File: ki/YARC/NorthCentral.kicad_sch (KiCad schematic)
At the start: 10 parts, among them U102 74HC245, U103 74HC245, U106 74LS139, U128 74LS157, U132 74LS157, U133 74LS21, U134 74LS32, U138 74LS14, U146 74LS574, U93 74LS32

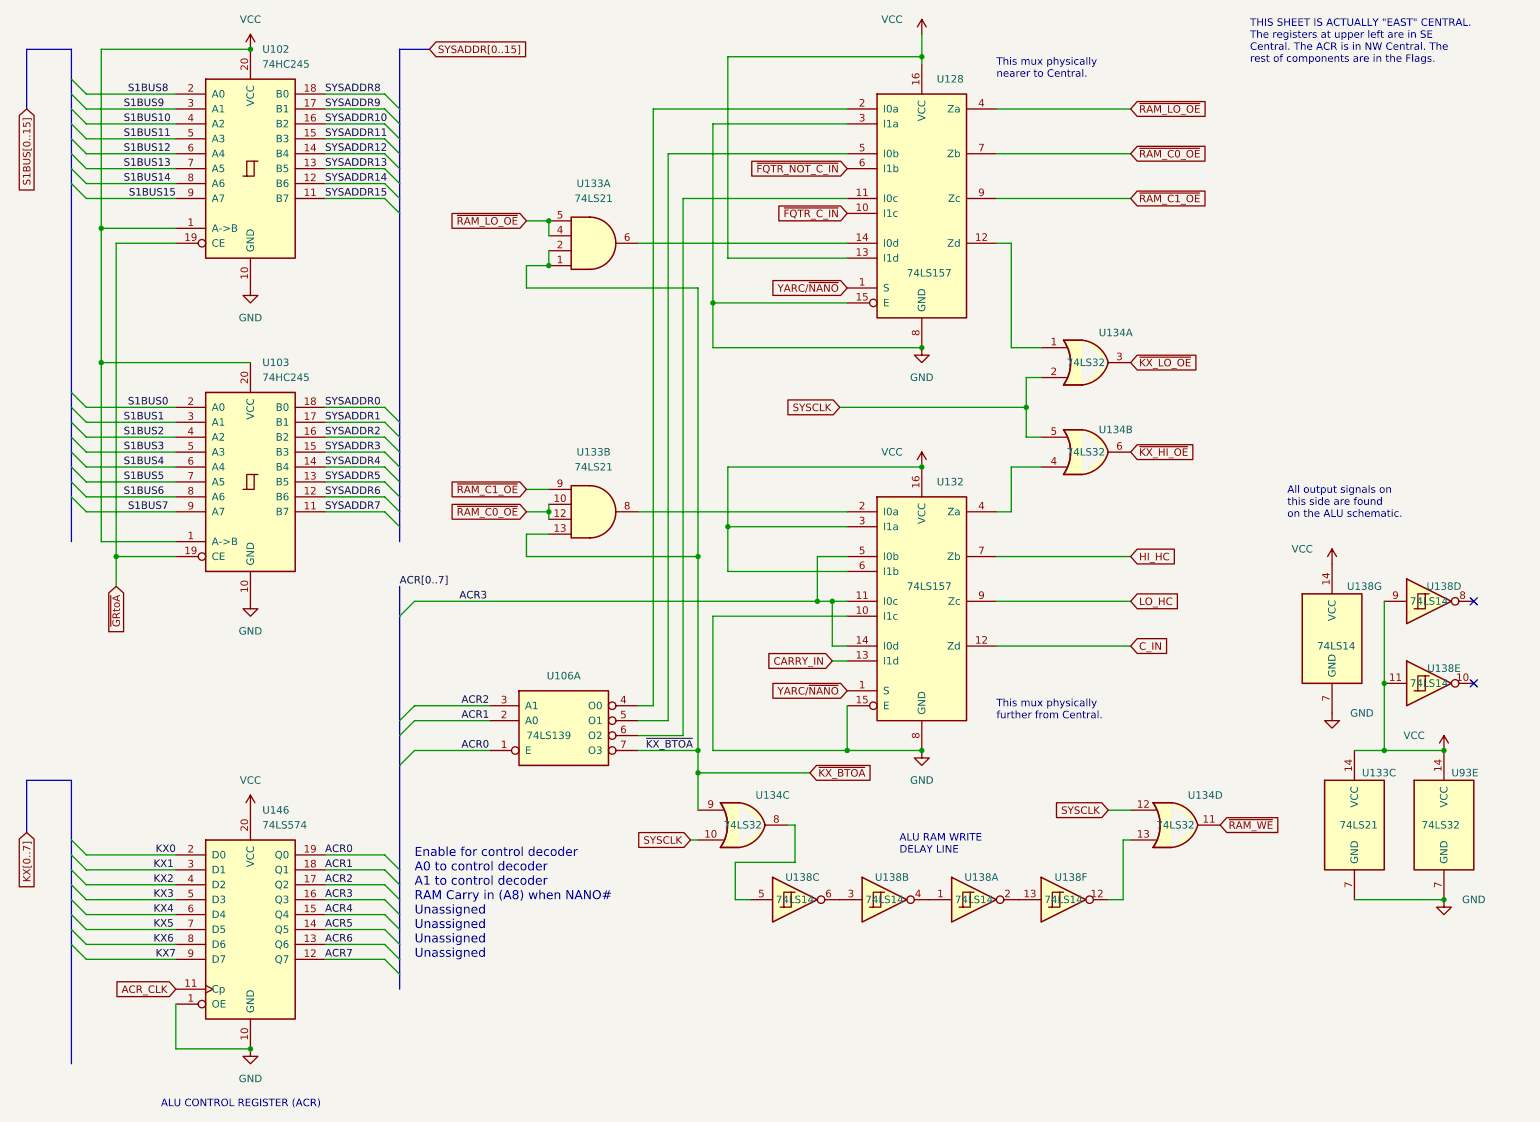
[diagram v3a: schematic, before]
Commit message: Schematic for addressing unit is complete and all ERC violations addressed
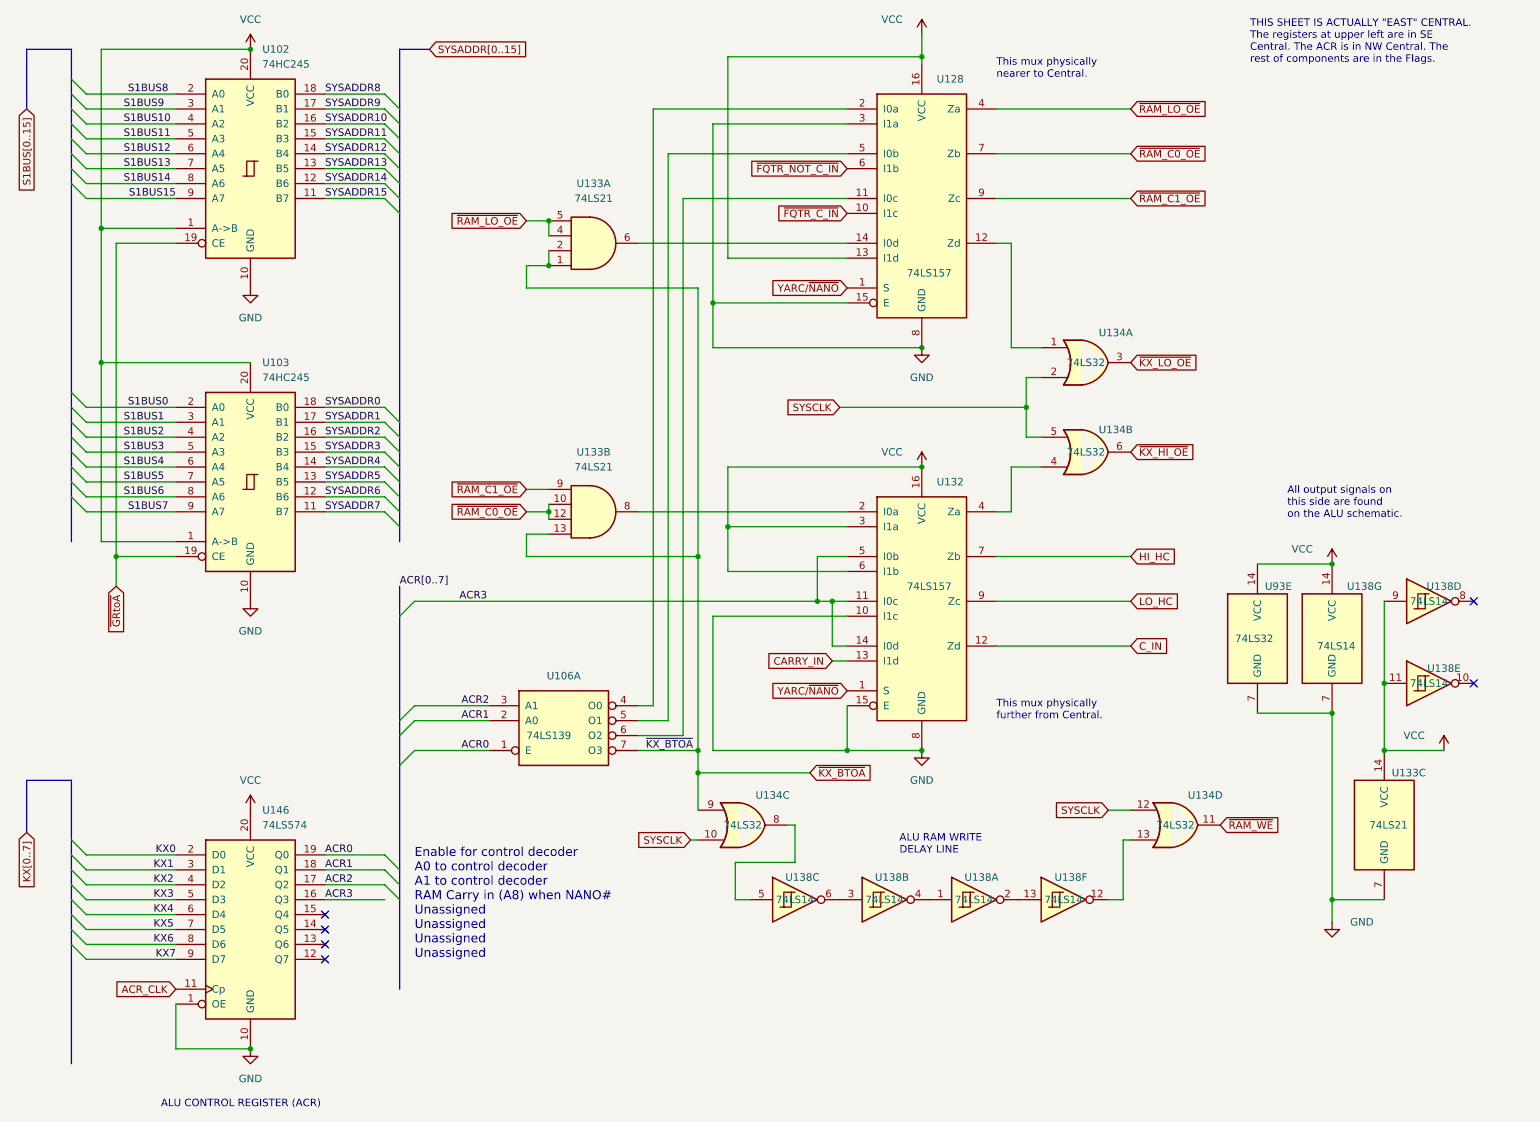
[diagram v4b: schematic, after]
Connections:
- net ACR4: no longer names the net of U146.15 (Q4)
- net ACR5: no longer names the net of U146.14 (Q5)
- net ACR6: no longer names the net of U146.13 (Q6)
- net ACR7: no longer names the net of U146.12 (Q7)
- no-connect marks 2 -> 6
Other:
- moved on the sheet: U133C
